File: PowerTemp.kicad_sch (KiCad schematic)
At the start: 22 parts, among them U33 74HC123, U70 LMV321, U71 LMV321

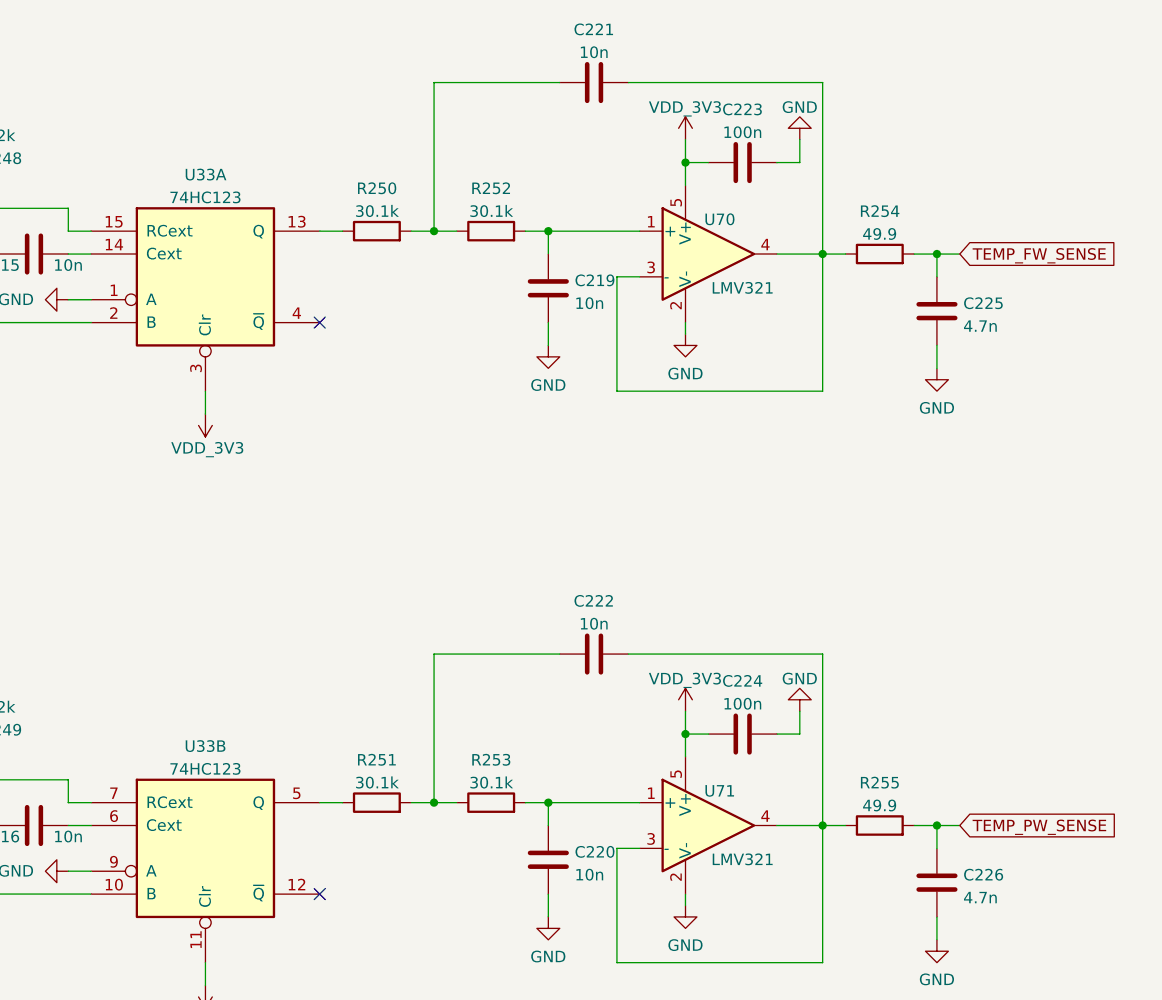
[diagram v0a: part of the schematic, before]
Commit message: Изменения в схеме: убрал разъемы датчиков тока
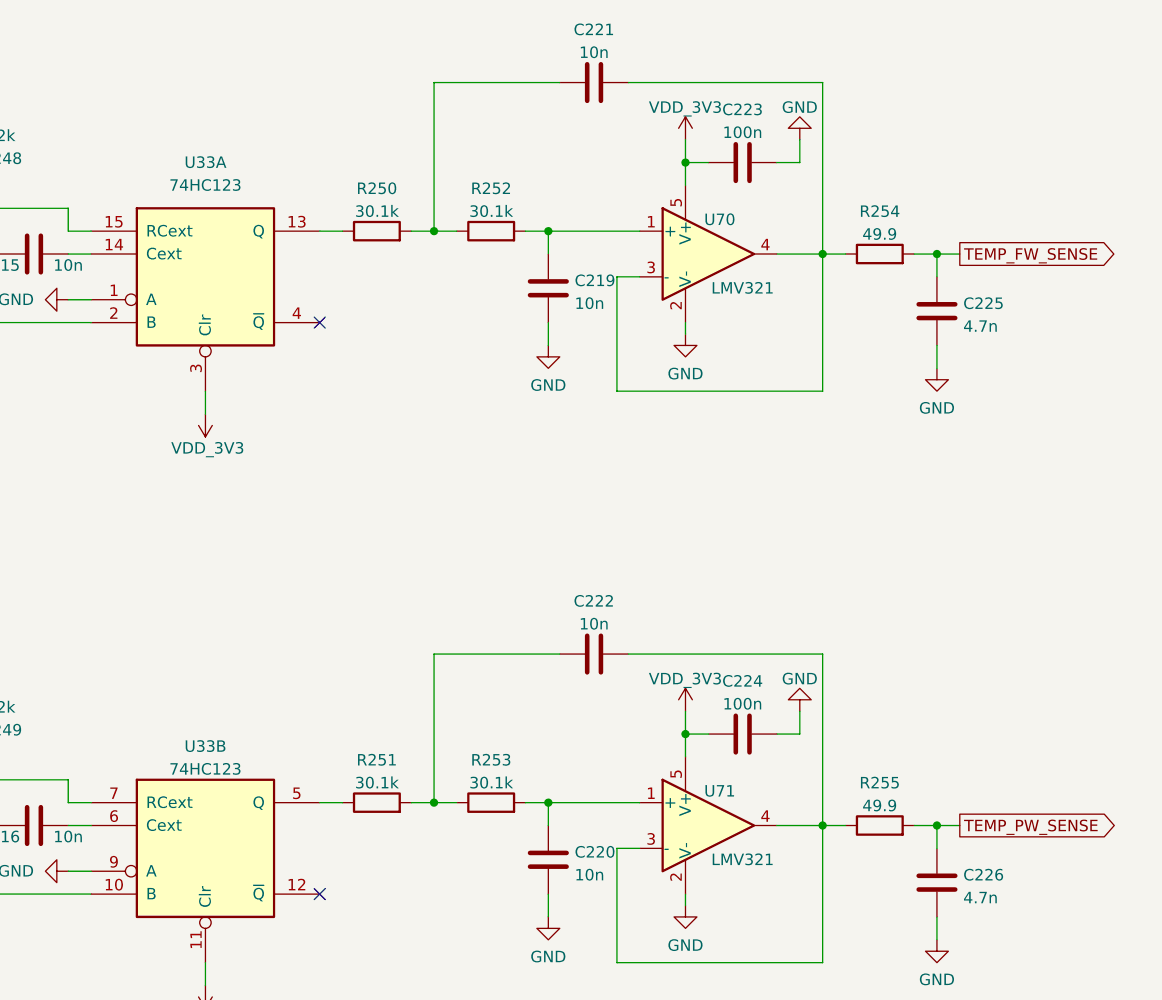
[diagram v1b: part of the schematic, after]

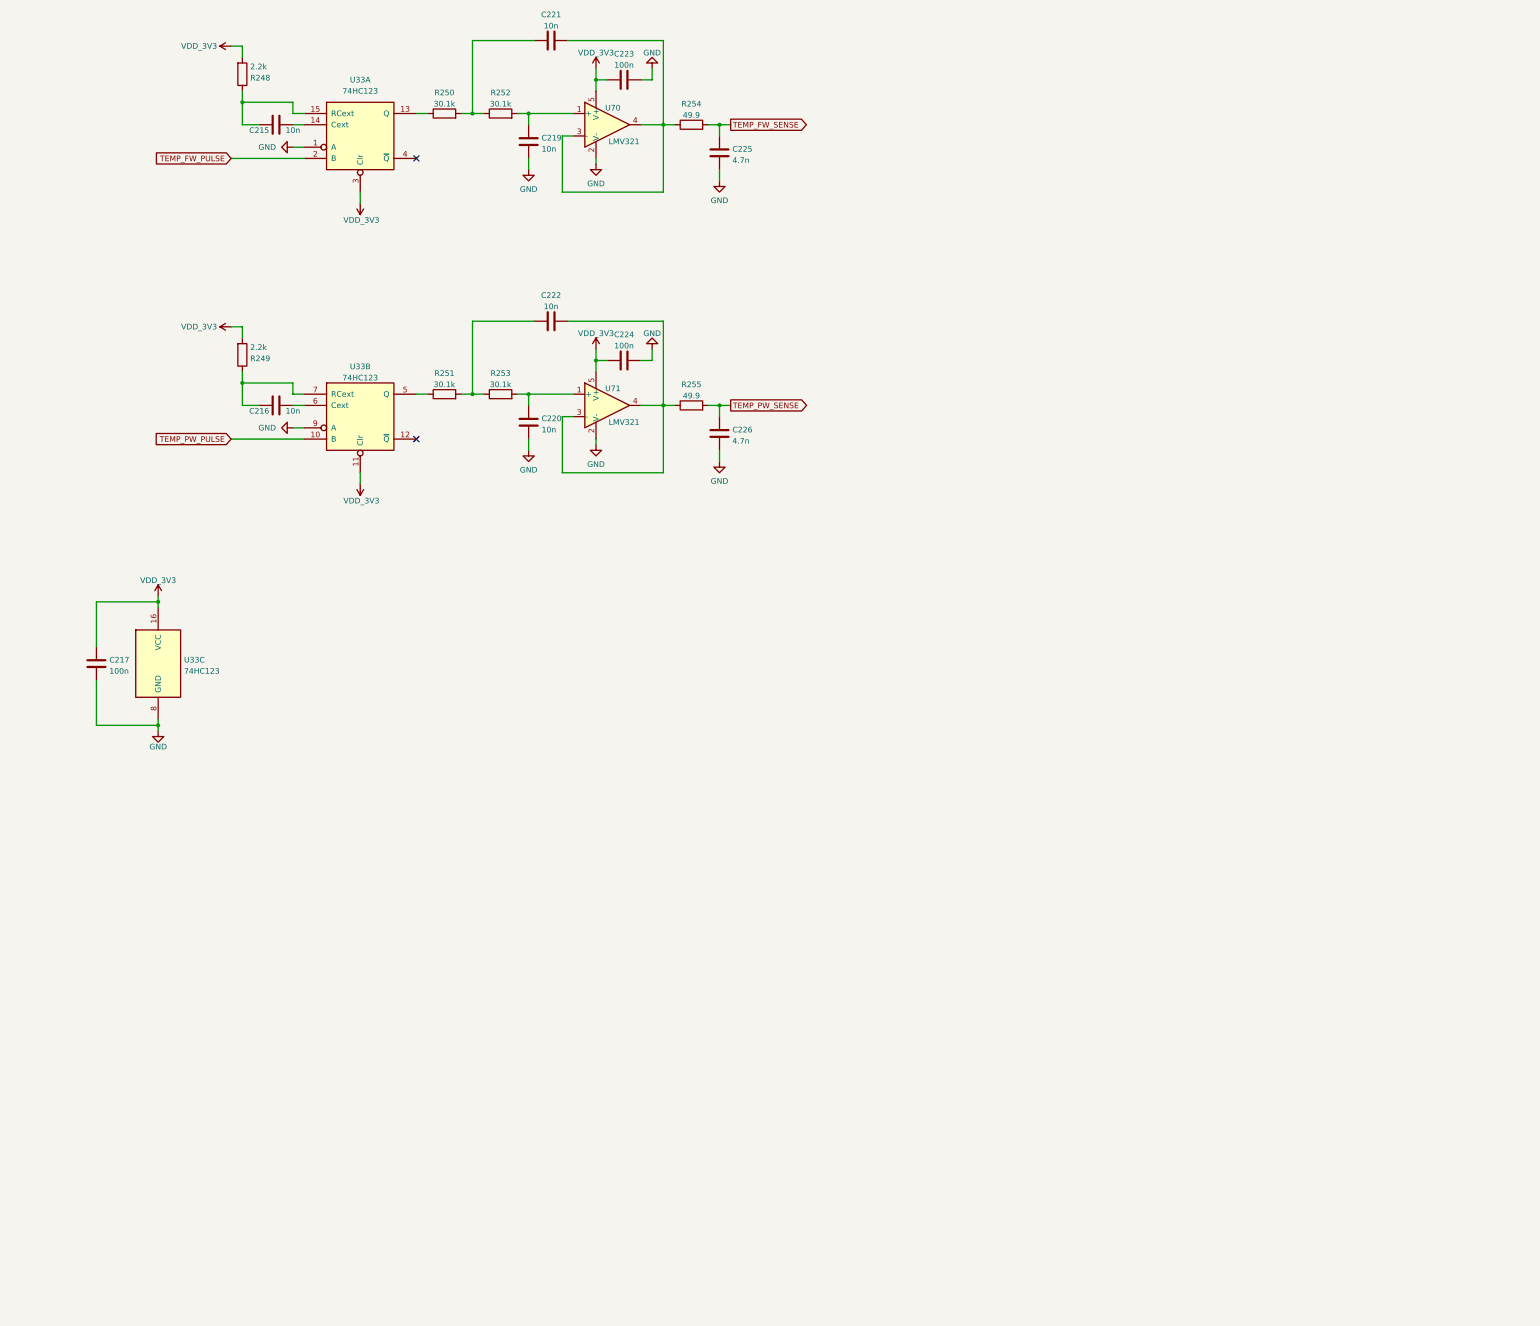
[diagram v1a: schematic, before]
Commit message: Исправление: в схеме добавил обработку температур, изменил обработку токов
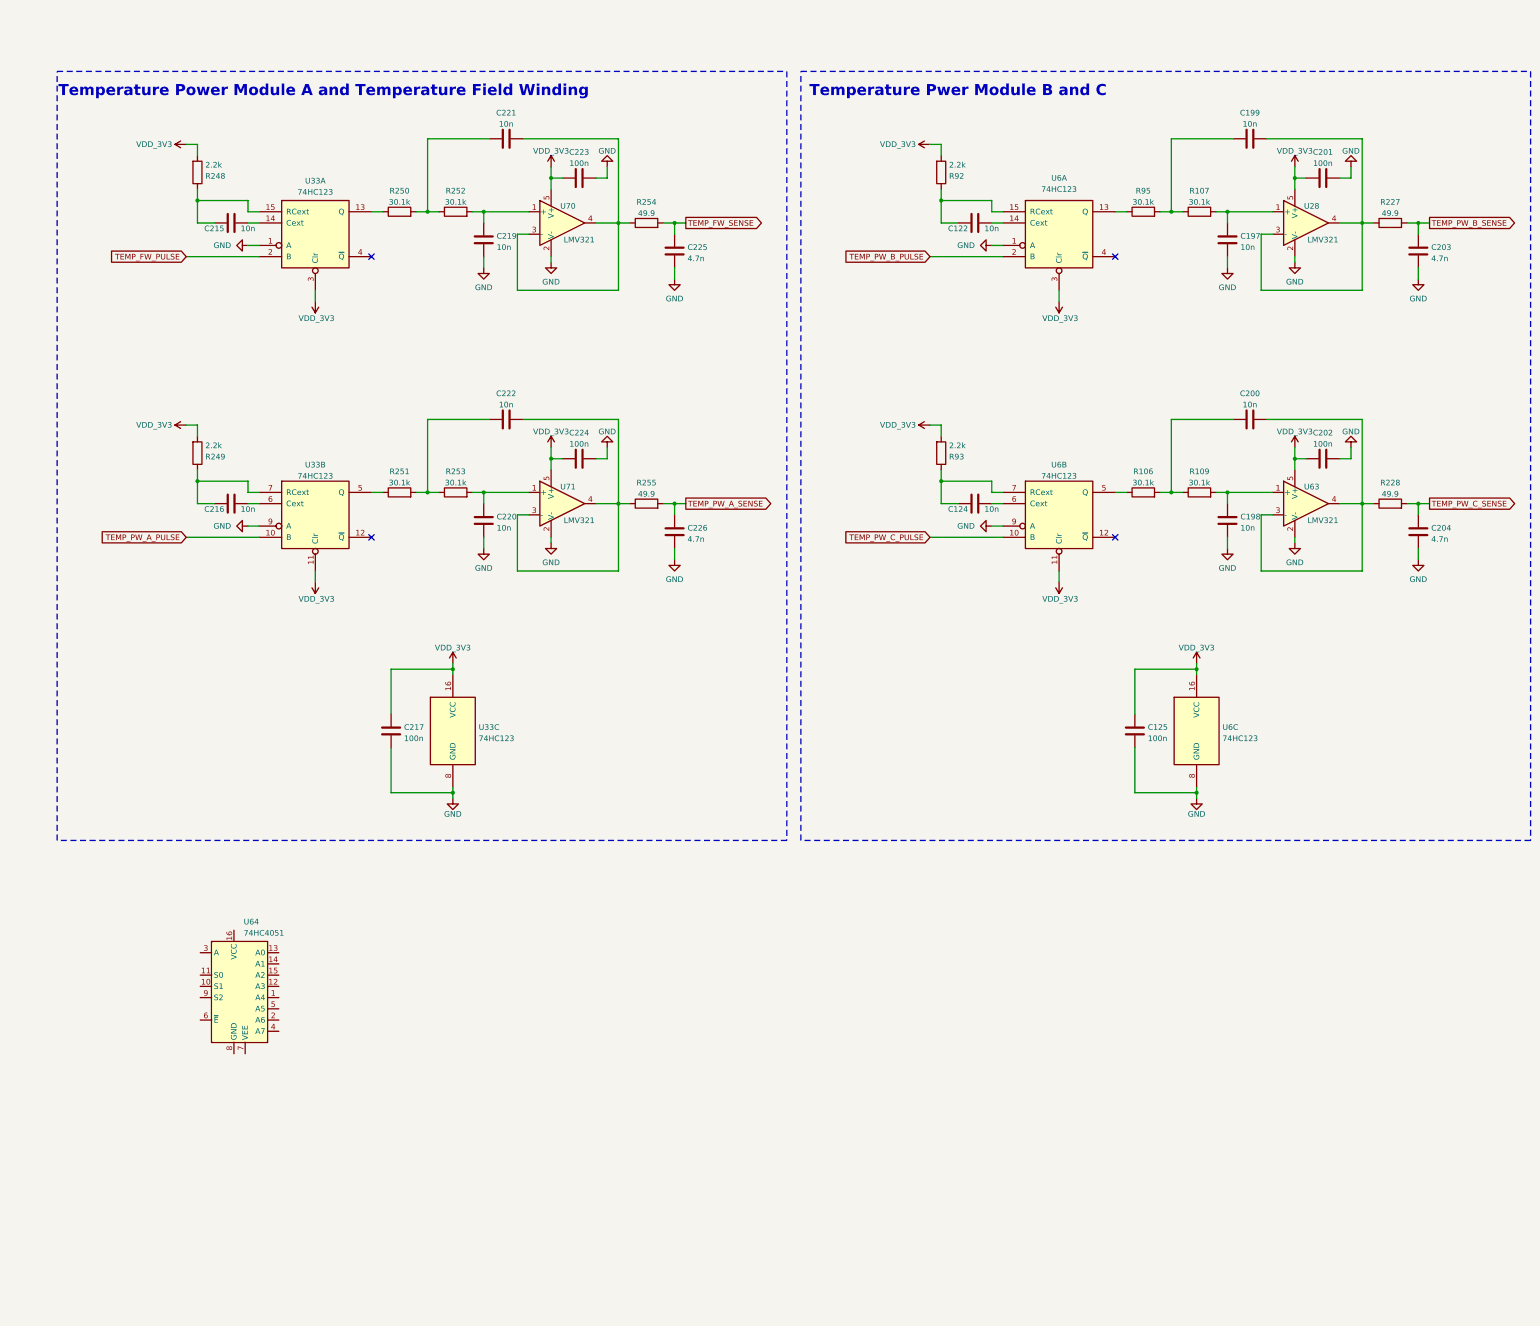
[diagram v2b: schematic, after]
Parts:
- added C122, C124, C197, C198, C199, C200: 10n, Capacitor_SMD:C_0603_1608Metric, symbol Device:C
- added C125, C201, C202: 100n, Capacitor_SMD:C_0603_1608Metric, symbol Device:C
- added C203, C204: 4.7n, Capacitor_SMD:C_0603_1608Metric, symbol Device:C
- added R106, R107, R109, R95: 30.1k, Resistor_SMD:R_0603_1608Metric, symbol Device:R
- added R227, R228: 49.9, Resistor_SMD:R_0603_1608Metric, symbol Device:R
- added R92, R93: 2.2k, Resistor_SMD:R_0603_1608Metric, symbol Device:R
- added U28, U63: LMV321, Package_TO_SOT_SMD:SOT-23-5, symbol Amplifier_Operational:LMV321
- added U6: 74HC123, Package_SO:SO-16_3.9x9.9mm_P1.27mm, symbol 74xx:74HC123
- added U64: 74HC4051, symbol 74xx:74HC4051
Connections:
- net GND: now also C125.1, C197.2, C198.2, C201.2, C202.2, C203.2, C204.2, U28.2 (V-), U6.1 (A), U6.8 (GND), U6.9 (A), U63.2 (V-)
- net VDD_3V3: now also C125.2, C201.1, C202.1, R92.2, R93.2, U28.5 (V+), U6.11 (Clr), U6.16 (VCC), U6.3 (Clr), U63.5 (V+)
- net TEMP_PW_PULSE renamed TEMP_PW_A_PULSE
- net TEMP_PW_SENSE renamed TEMP_PW_A_SENSE
- new net: R106.1, U6.5 (Q)
- new net: C200.1, R106.2, R109.1
- new net: C198.1, R109.2, U63.1 (+)
- new net: C200.2, R228.1, U63.3 (-), U63.4
- new net: C124.1, R93.1, U6.7 (RCext)
- new net: C122.1, R92.1, U6.15 (RCext)
- new net: C122.2, U6.14 (Cext)
- new net: C199.1, R107.1, R95.2
- new net: C197.1, R107.2, U28.1 (+)
- new net: C124.2, U6.6 (Cext)
- new net: C199.2, R227.1, U28.3 (-), U28.4
- new net: R95.1, U6.13 (Q)
- new net TEMP_PW_B_PULSE: U6.2 (B)
- new net TEMP_PW_B_SENSE: C203.1, R227.2
- new net TEMP_PW_C_PULSE: U6.10 (B)
- new net TEMP_PW_C_SENSE: C204.1, R228.2
- no-connect marks 2 -> 4
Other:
- note added: "Temperature Power Module A and Temperature Field Winding"
- note added: "Temperature Pwer Module B and C"
- moved on the sheet: C215, C216, C217, C219, C220, C221, C222, C223, C224, C225, C226, R248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

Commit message: Добавления: Расставил все на плате
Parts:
- added C205: 100n, Capacitor_SMD:C_0603_1608Metric, symbol Device:C
- U64: footprint (none) -> Package_SO:SOIC-16_3.9x9.9mm_P1.27mm
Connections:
- net GND: now also U64.6 (~{E}), U64.7 (VEE), U64.8 (GND), C205.1
- net TEMP_PW_A_SENSE: now also U64.13 (A0)
- net TEMP_PW_B_SENSE: now also U64.14 (A1)
- net TEMP_PW_C_SENSE: now also U64.15 (A2)
- net VDD_3V3: now also U64.16 (VCC), C205.2
- net S1_TEMP_MULIPLEX: now reaches U64.10 (S1)
- net S0_TEMP_MULIPLEX: now reaches U64.11 (S0)
- net TEMP_PW_SENSE: now reaches U64.3 (A)
- net S2_TEMP_MULIPLEX: now reaches U64.9 (S2)
- no-connect marks 4 -> 9
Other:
- note added: "Temperature Power Module Multiplex"
- moved on the sheet: U64
